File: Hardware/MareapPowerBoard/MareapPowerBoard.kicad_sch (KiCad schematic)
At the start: 72 parts, among them J1 XT60PW-M, J10 Comp_Plus_Pin, J11 Comp_Minus_Pin, J12 5VConv_Pin, J13 Batt_Pin, J14 5VUSB_Pin, J15 PowerPins, J2 USB_C_Receptacle_USB2.0_16P, J3 USB_C_MALE, J4 SSD1306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

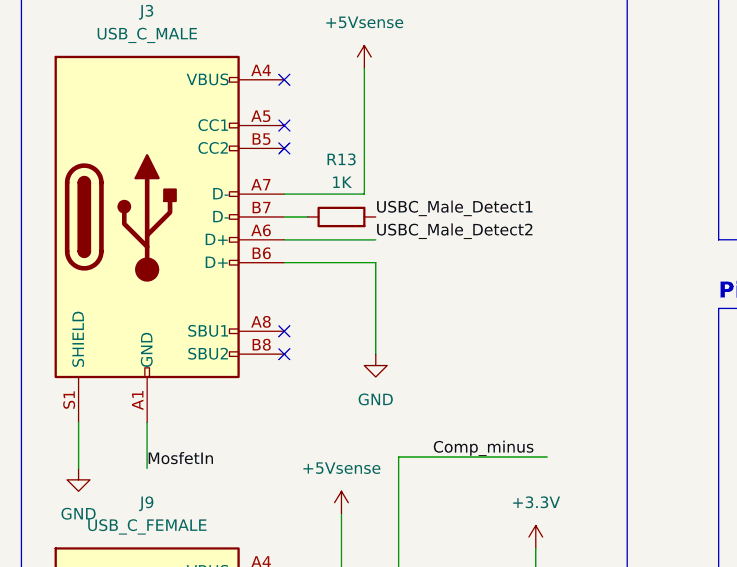
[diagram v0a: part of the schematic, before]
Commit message: added missing connection and r14 for noise filtering
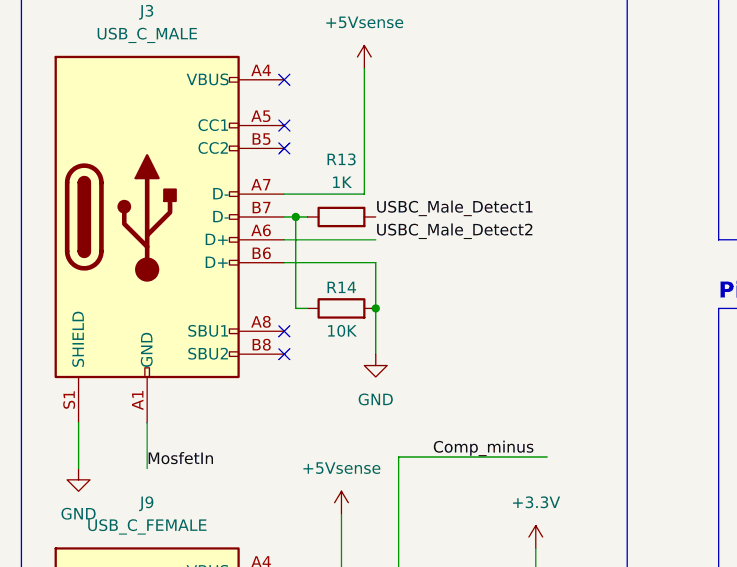
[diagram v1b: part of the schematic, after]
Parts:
- added R14: 10K, Resistor_SMD:R_0603_1608Metric, symbol Device:R
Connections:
- net GND: now also R14.2
- net at J3.B7 (D-), R13.1: now also R14.1
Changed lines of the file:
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@@
 	)
 	(junction
+		(at 44.45 149.86)
+		(diameter 0)
+		(color 0 0 0 0)
+	)
+	(junction
 		(at 22.86 101.6)
 		(diameter 0)
@@
 	)
 	(junction
+		(at 53.34 160.02)
+		(diameter 0)
+		(color 0 0 0 0)
+	)
+	(junction
 		(at 168.91 40.64)
 		(diameter 0)
@@
 	(wire
 		(pts
+			(xy 53.34 160.02) (xy 53.34 165.1)
+		)
+		(stroke
+			(width 0)
+			(type default)
+		)
+	)
+	(wire
+		(pts
 			(xy 127 62.23) (xy 116.84 62.23)
 		)
@@
 	(wire
 		(pts
-			(xy 43.18 149.86) (xy 45.72 149.86)
+			(xy 43.18 149.86) (xy 44.45 149.86)
 		)
 		(stroke
@@
 	(wire
 		(pts
+			(xy 45.72 160.02) (xy 44.45 160.02)
+		)
+		(stroke
+			(width 0)
+			(type default)
+		)
+	)
+	(wire
+		(pts
 			(xy 132.08 40.64) (xy 121.92 40.64)
 		)
@@
 	(wire
 		(pts
+			(xy 44.45 149.86) (xy 45.72 149.86)
+		)
+		(stroke
+			(width 0)
+			(type default)
+		)
+	)
+	(wire
+		(pts
 			(xy 146.05 76.2) (xy 111.76 76.2)
 		)
@@
 	(wire
 		(pts
+			(xy 44.45 160.02) (xy 44.45 149.86)
+		)
+		(stroke
+			(width 0)
+			(type default)
+		)
+	)
+	(wire
+		(pts
 			(xy 151.13 50.8) (xy 151.13 54.61)
 		)
@@
 	(wire
 		(pts
-			(xy 53.34 154.94) (xy 53.34 165.1)
+			(xy 53.34 154.94) (xy 53.34 160.02)
 		)
 		(stroke
@@
 					(unit 1)
 				)
+			)
+		)
+	)
+	(symbol
+		(lib_id "Device:R")
+		(at 49.53 160.02 90)
+		(unit 1)
+		(body_style 1)
+		(exclude_from_sim no)
+		(in_bom yes)
+		(on_board yes)
+		(in_pos_files yes)
+		(dnp no)
+		(property "Reference" "R14"
+			(at 49.53 157.734 90)
+			(show_name no)
+			(do_not_autoplace no)
+			(effects
+				(font
+					(size 1.27 1.27)
+				)
+			)
+		)
+		(property "Value" "10K"
+			(at 49.53 162.56 90)
+			(show_name no)
+			(do_not_autoplace no)
+			(effects
+				(font
+					(size 1.27 1.27)
+				)
+			)
+		)
+		(property "Footprint" "Resistor_SMD:R_0603_1608Metric"
+			(at 49.53 161.798 90)
+			(hide yes)
+			(show_name no)
+			(do_not_autoplace no)
+			(effects
+				(font
+					(size 1.27 1.27)
+				)
+			)
+		)
+		(property "Datasheet" ""
+			(at 49.53 160.02 0)
+			(hide yes)
+			(show_name no)
+			(do_not_autoplace no)
+			(effects
+				(font
+					(size 1.27 1.27)
+				)
+			)
+		)
+		(property "Description" "Resistor"
+			(at 49.53 160.02 0)
+			(hide yes)
+			(show_name no)
+			(do_not_autoplace no)
+			(effects
+				(font
+					(size 1.27 1.27)
+				)
+			)
+		)
+		(pin "1"
+		)
+		(pin "2"
+		)
+		(instances
+			(project "MareapPowerBoard"
+				(path "/7470ac58-41ff-4b7f-84e3-8e3819efdbb2"
+					(reference "R14")
+					(unit 1)
+				)
